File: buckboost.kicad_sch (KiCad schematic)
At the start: 18 parts, among them Q1 AO3400A, Q2 AO3400A, Q3 AO3400A, Q4 AO3400A, U6 L6388E

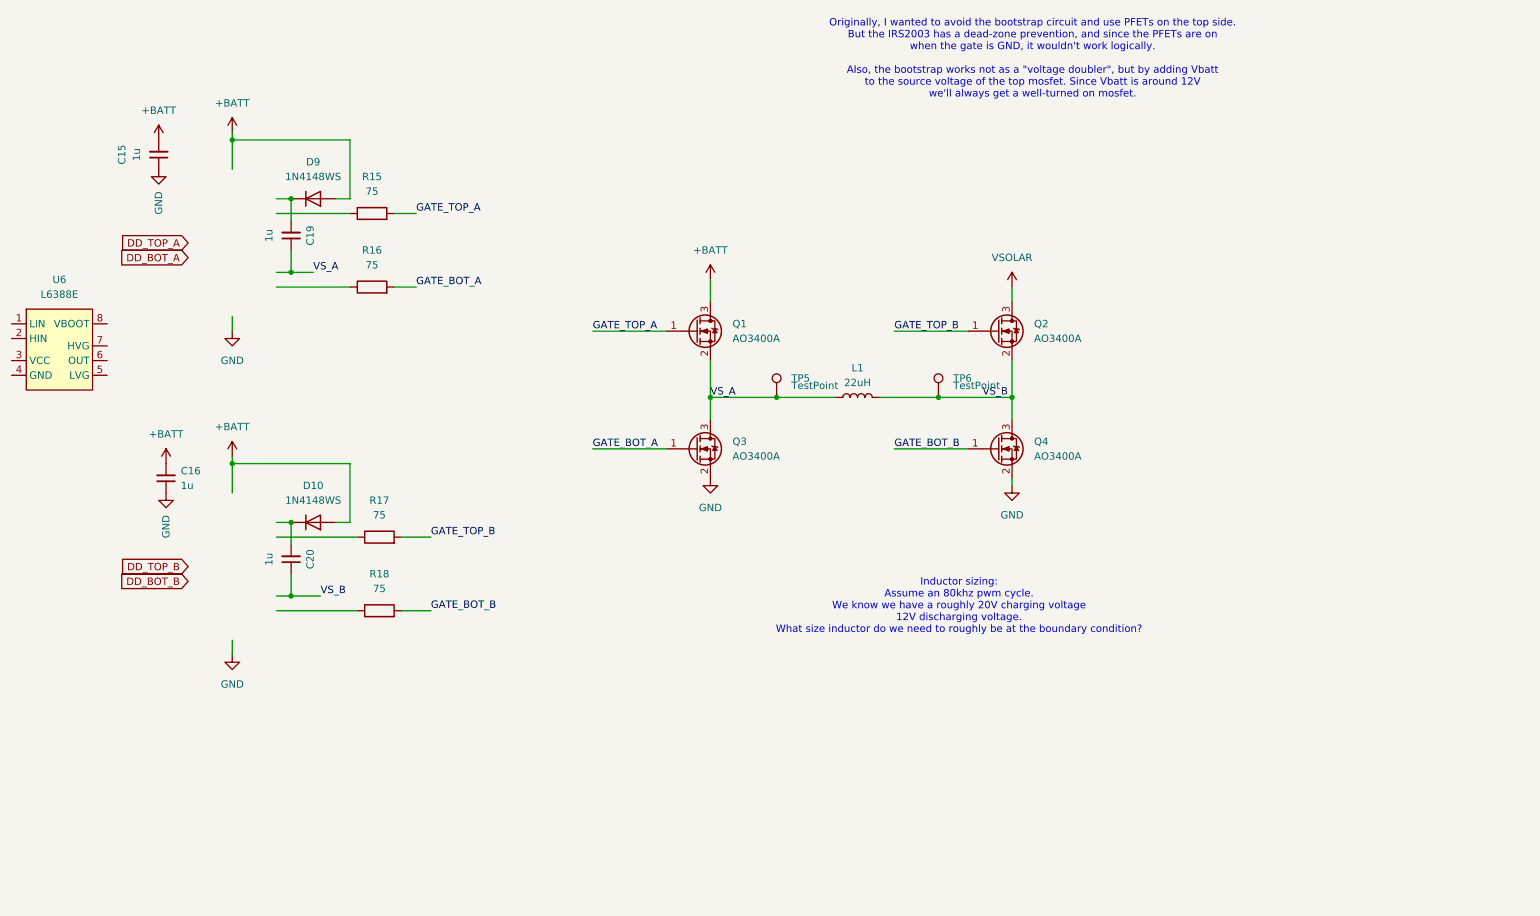
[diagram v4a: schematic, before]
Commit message: L6388E mosfet drivers
Allow to enable/disable drivers
voltage dividers picked out
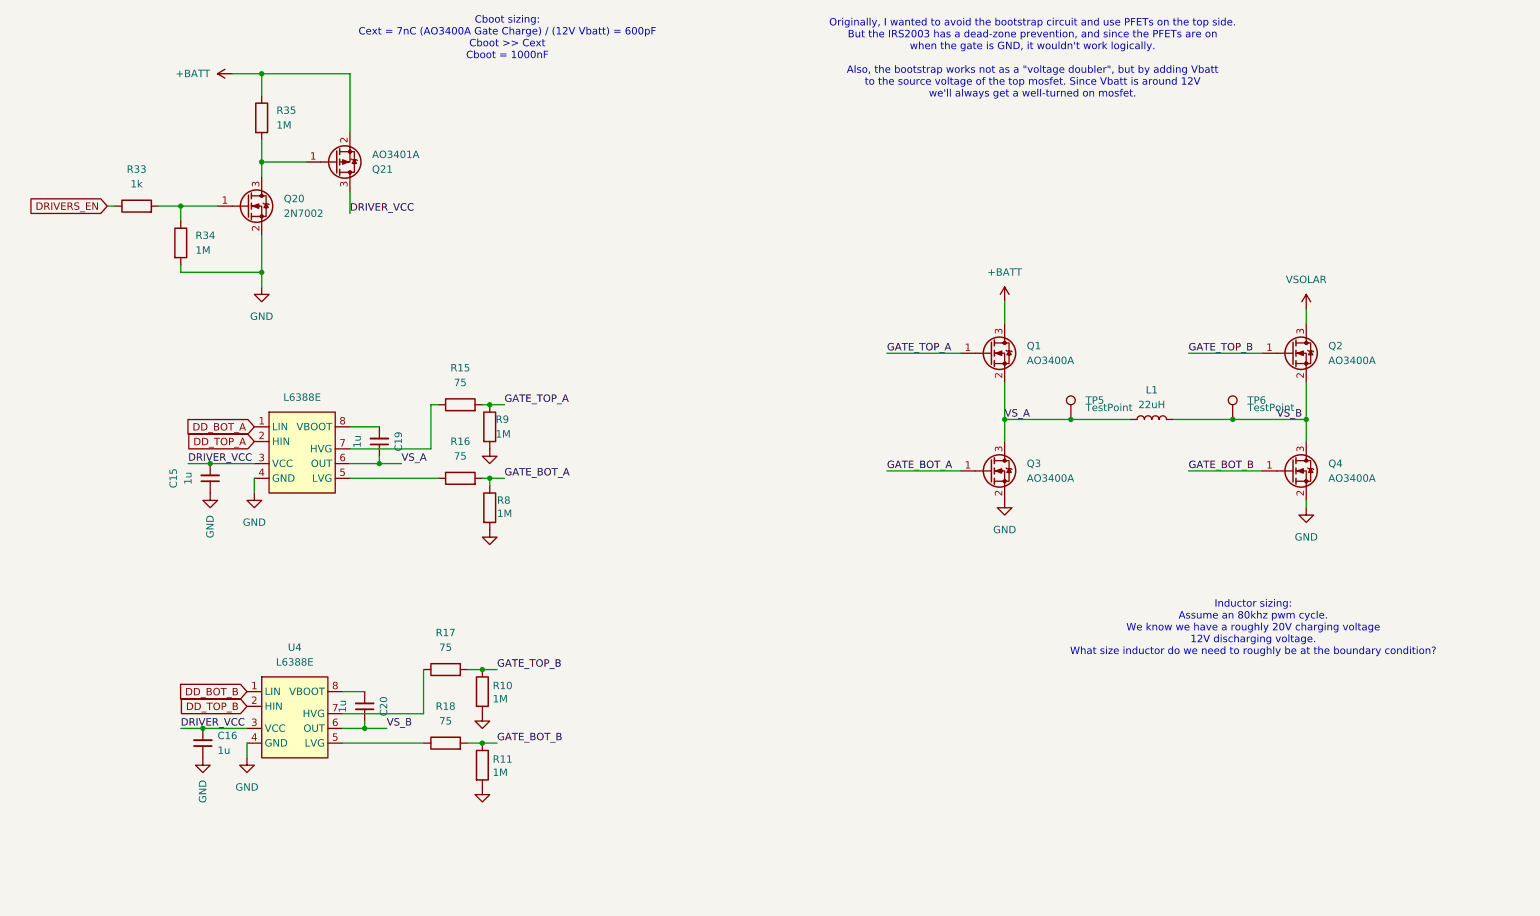
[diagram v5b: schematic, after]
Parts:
- removed D10, D9: 1N4148WS, Diode_SMD:D_SOD-323, symbol Diode:1N4148WS
- added Q20: 2N7002, Package_TO_SOT_SMD:SOT-323_SC-70, symbol Transistor_FET:2N7002
- added Q21: AO3401A, Package_TO_SOT_SMD:SOT-23, symbol Transistor_FET:AO3401A
- added R10, R11, R34, R35, R8, R9: 1M, Resistor_SMD:R_0603_1608Metric, symbol Device:R
- added R33: 1k, Resistor_SMD:R_0603_1608Metric, symbol Device:R
- added U4: L6388E, Package_SO:SO-8_3.9x4.9mm_P1.27mm, symbol JakeLib:L6388E
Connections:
- net +BATT: now also Q21.2 (S), R35.1; no longer C15.2, C16.2
- net DD_BOT_A: now also U6.1 (LIN)
- net DD_BOT_B: now also U4.1 (LIN)
- net DD_TOP_A: now also U6.2 (HIN)
- net DD_TOP_B: now also U4.2 (HIN)
- net GATE_BOT_A: now also R8.1
- net GATE_BOT_B: now also R11.1
- net GATE_TOP_A: now also R9.1
- net GATE_TOP_B: now also R10.1
- net GND: now also U6.4 (GND), Q20.2 (S), R10.2, R11.2, R34.2, R8.2, R9.2, U4.4 (GND)
- net VS_A: now also U6.6 (OUT)
- net VS_B: now also U4.6 (OUT)
- net at R17.1: now also U4.7 (HVG)
- net at C20.2: now also U4.8 (VBOOT)
- net at R15.1: now also U6.7 (HVG)
- net DRIVER_VCC: now reaches U6.3 (VCC)
- net DRIVER_VCC: now also C15.2, C16.2, Q21.3 (D), U4.3 (VCC)
- net at U6.5 (LVG): now also R16.1
- net at U6.8 (VBOOT): now also C19.2
- net at R18.1: now also U4.5 (LVG)
- new net: Q20.1 (G), R33.2, R34.1
- new net: Q20.3 (D), Q21.1 (G), R35.2
- new net DRIVERS_EN: R33.1
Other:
- note added: "Cboot sizing: Cext = 7nC (AO3400A Gate Charge) / (12V Vbatt) = 600pF Cboot >> Cext Cboot = 1000nF"
- moved on the sheet: C15, C16, C19, C20, L1, Q1, Q2, Q3, Q4, R15, R16, R17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

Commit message: New schematic done
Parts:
- removed L1: 22uH, JakeLib:YSPI0630A, symbol Device:L
- added D2: BAT54SW, Package_TO_SOT_SMD:SOT-323_SC-70, symbol Diode:BAT54SW
- added L2: 68uH, Inductor_SMD:L_SXN_SMDRI127, symbol Device:L
- added R36: 7500, Resistor_SMD:R_0603_1608Metric, symbol Device:R
- added R37: 1600, Resistor_SMD:R_0603_1608Metric, symbol Device:R
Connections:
- net GND: now also D2.1 (A), R37.2
- net VS_A: now also L2.1, R36.1
- net VS_B: now also L2.2
- new net COMP2_INP: D2.3 (COM), R36.2, R37.1
- new net VDD: D2.2 (K)
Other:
- note added: "Cboot sizing: AO3400A Gate Charge = 7nC max Cext = 7nC / (12V Vbatt) = 600pF Cboot >> Cext Cboot = 1000nF"
- note added: "Inductor sizing: Assume an 80khz pwm cycle. We know we have a roughly 20V charging voltage 12V discharging voltage. Need around 60uH for BCM operation"
- note added: "Vrefint = 1.224V We want the comparator to trigger when VS_A is around 6V (or half the expected 12V) So we can have a backup measurement on when DCM mode is done"
- note removed: "Cboot sizing: Cext = 7nC (AO3400A Gate Charge) / (12V Vbatt) = 600pF Cboot >> Cext Cboot = 1000nF"
- note removed: "Inductor sizing: Assume an 80khz pwm cycle. We know we have a roughly 20V charging voltage 12V discharging voltage. What size inductor do we need to roughly be at the boundary condition?"
- moved on the sheet: Q1, Q2, Q3, Q4, TP5, TP6

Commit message: A couple of part selections
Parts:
- L2: value 68uH -> 47uH; footprint Inductor_SMD:L_SXN_SMDRI127 -> Inductor_SMD:L_Sunlord_MWSA0605S; LCSC_Code C9907 -> C408471
- R36: LCSC_Code (none) -> C23234
- R37: LCSC_Code (none) -> C22847
- U4, U6: LCSC_Code (none) -> C23921
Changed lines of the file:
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@@
 			)
 		)
+		(property "LCSC_Code" "C23921"
+			(at 72.39 142.24 0)
+			(effects
+				(font
+					(size 1.27 1.27)
+				)
+				(hide yes)
+			)
+		)
 		(pin "1"
 		)
@@
 			)
 		)
-		(property "Value" "68uH"
+		(property "Value" "47uH"
 			(at 210.82 88.9 90)
 			(effects
@@
 			)
 		)
-		(property "Footprint" "Inductor_SMD:L_SXN_SMDRI127"
+		(property "Footprint" "Inductor_SMD:L_Sunlord_MWSA0605S"
 			(at 210.82 91.44 0)
 			(effects
@@
 			)
 		)
-		(property "Datasheet" "https://datasheet.lcsc.com/lcsc/2108131530_SXN-Shun-Xiang-Nuo-Elec-SMDRI127-680MT_C9907.pdf"
+		(property "Datasheet" "https://datasheet.lcsc.com/lcsc/2310251550_Sunlord-MWSA0605S-470MT_C408471.pdf"
 			(at 210.82 91.44 0)
 			(effects
@@
 			)
 		)
-		(property "Description" "2.1A 68uH Shielded Power Inductors ±20% 4A SMD,12.3x12.3mm"
+		(property "Description" "  2A 47uH ±20% 2.6A SMD,7x6.6mm Power Inductors ROHS "
 			(at 210.82 91.44 0)
 			(effects
@@
 			)
 		)
-		(property "LCSC_Code" "C9907"
+		(property "LCSC_Code" "C408471"
 			(at 210.82 91.44 90)
 			(effects
@@
 			)
 		)
+		(property "LCSC_Code" "C23921"
+			(at 73.66 96.52 0)
+			(effects
+				(font
+					(size 1.27 1.27)
+				)
+				(hide yes)
+			)
+		)
 		(pin "1"
 		)
@@
 			)
 		)
+		(property "LCSC_Code" "C22847"
+			(at 175.26 146.05 0)
+			(effects
+				(font
+					(size 1.27 1.27)
+				)
+				(hide yes)
+			)
+		)
 		(pin "2"
 		)
@@
 			(at 175.26 135.89 0)
 			(effects
+				(font
+					(size 1.27 1.27)
+				)
+				(hide yes)
+			)
+		)
+		(property "LCSC_Code" "C23234"
+			(at 175.26 135.89 0)
+			(effects

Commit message: Decent pass
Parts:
- renumbered C15 to C17, C20 to C18, D2 to D12, L2 to L1, Q20 to Q1, Q21 to Q2, Q1 to Q3, Q3 to Q4, Q2 to Q5, Q4 to Q6, R33 to R12, R34 to R13, R35 to R14, R17 to R15, R18 to R16, R15 to R17, R16 to R18, R10 to R19, R11 to R20, R9 to R21, R8 to R22, R36 to R23, R37 to R24, TP5 to TP3, TP6 to TP4, U6 to U5
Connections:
- net GND: no longer R19.2, R21.2
- net VS_A: now also R21.2
- net VS_B: now also R19.2
